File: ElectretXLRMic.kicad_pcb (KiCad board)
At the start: 2 copper layers, 37 x 52 mm, 38 parts, among them IC1 OPA1678IDR, J1 MIC, J2 XLR3

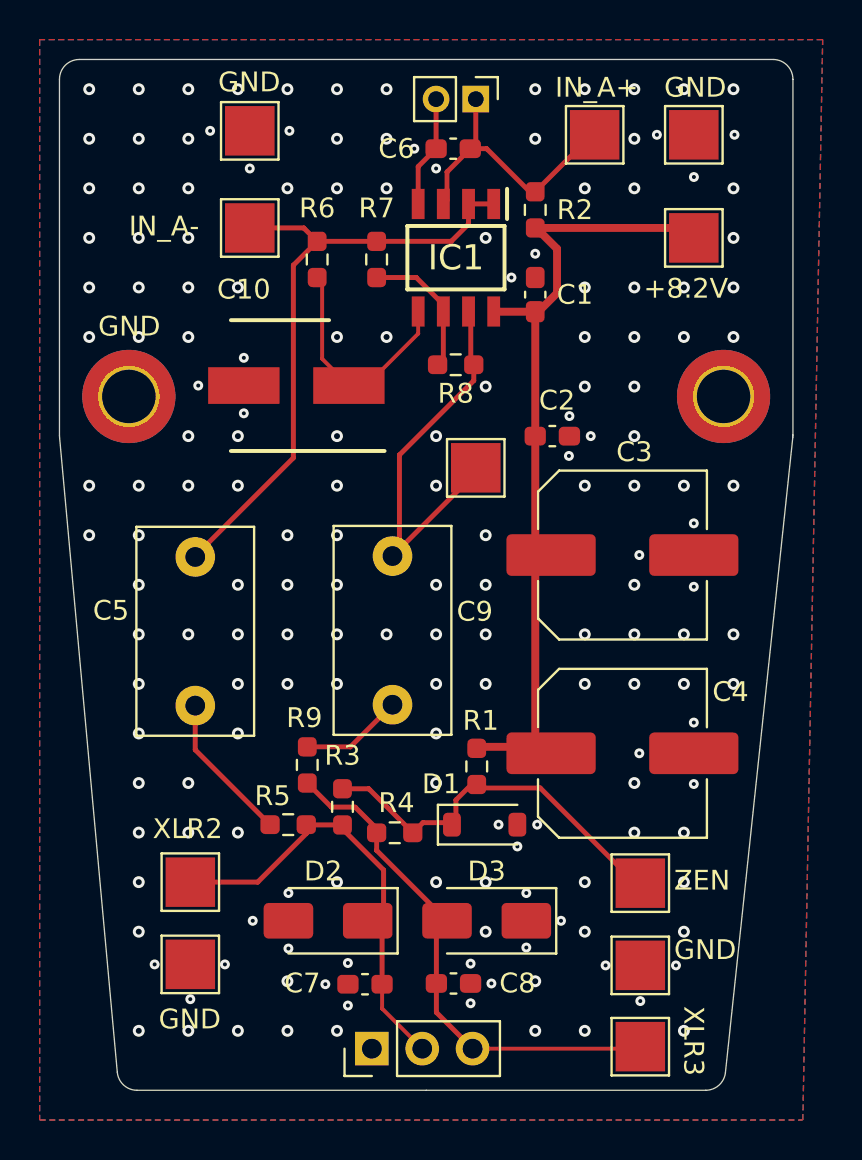
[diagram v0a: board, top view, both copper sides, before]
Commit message: Slight layout improvements
[KiCad Version: 9.0.7]
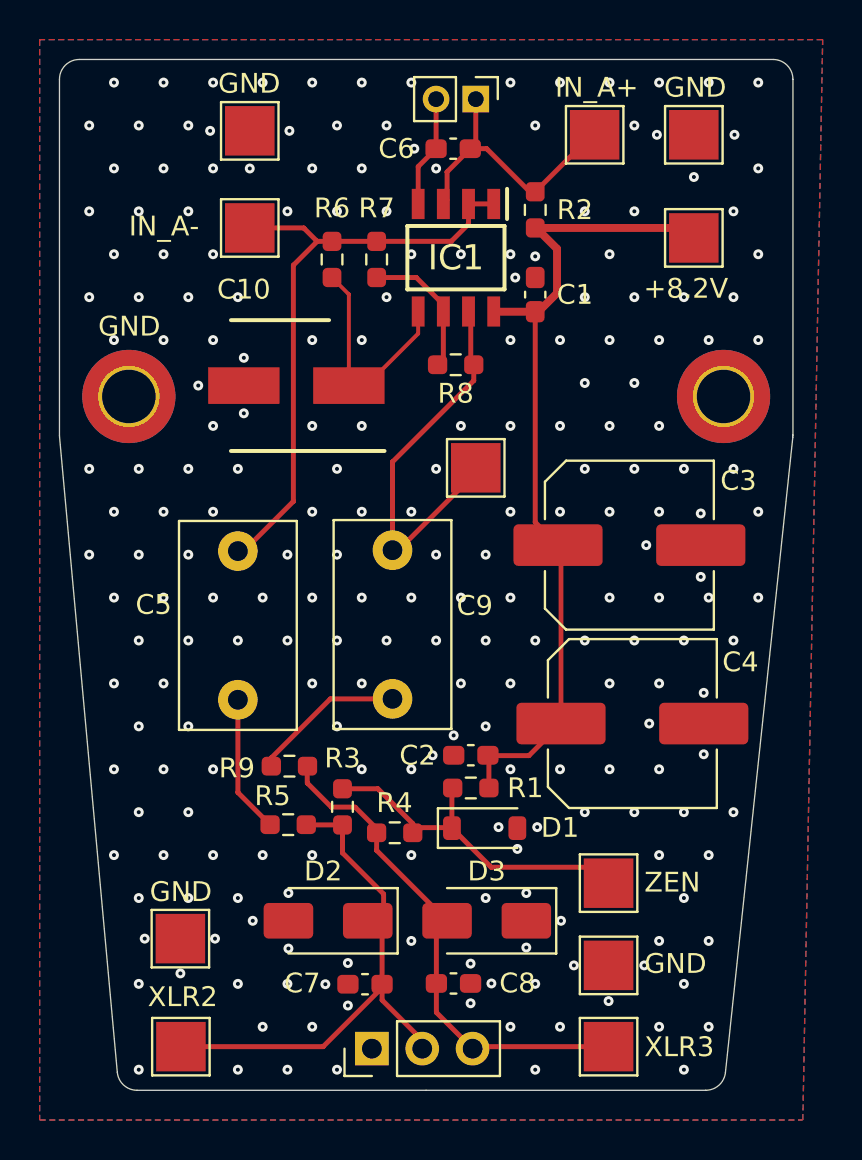
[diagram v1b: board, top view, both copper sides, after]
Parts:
- moved C2 16.6 mm to (110.8, 90.1), turned to 180 degrees
- moved TP9 8.31 mm to (96.1, 104.8)
- moved C5 2.17 mm to (99.0, 87.3)
- moved TP11 1.60 mm to (117.7, 104.8)
- moved TP2 1.60 mm to (117.7, 96.5)
- moved TP3 1.60 mm to (117.7, 100.7)
- moved C4 1.58 mm to (118.9, 88.5)
- moved TP6 1.39 mm to (96.1, 99.3)
- moved R1 1.13 mm to (110.8, 91.8), turned to 0 degrees
- moved R9 0.90 mm to (101.6, 90.7), turned to 0 degrees
- moved R6 0.75 mm to (103.8, 65.1)
- moved C3 0.61 mm to (118.8, 79.5)
- moved C9 0.30 mm to (106.8, 79.8)
- moved D1 0.18 mm to (111.5, 93.8)
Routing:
- net Net-(D2-A1): track 22.8 -> 27.0 mm
- net Net-(C9-Pad2): track 5.18 -> 8.06 mm
- net Net-(D1-K): track 19.4 -> 17.9 mm
- net Net-(C5-Pad1): track 7.61 -> 6.68 mm
- net Net-(D3-A2): track 26.5 -> 25.8 mm
- net V-: track 6.28 -> 6.13 mm, vias 177 -> 229
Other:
- board text added: "The Phantom of the Op-Amp 15.3.2026 M.H."
- board text added: "Tune OUTA to half of VCC with R2 value"
- board text removed: "The Phantom of the Op-Amp 2.3.2026 M.H."
- board text removed: "Tune OUTA to half of VCC with R2 value Match C12 and C13 closely"

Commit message: Cleaned up repo, small changes to PCB layout
[KiCad Version: 9.0.7]
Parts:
- moved TP5 28.2 mm to (94.2, 86.2)
- moved TP8 17.1 mm to (94.2, 79.8)
- moved C10 1.19 mm to (103.0, 72.0), turned to -90 degrees
- moved R9 0.97 mm to (102.5, 91.0), turned to -90 degrees
- moved C5 0.75 mm to (99.8, 87.3)
- moved C9 0.70 mm to (107.5, 79.8)
- moved TP10 0.40 mm to (111.0, 76.0)
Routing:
- net OUT_B: track 20.3 -> 13.6 mm
- net +IN_B: track 11.5 -> 9.54 mm
- net Net-(C9-Pad2): track 8.06 -> 6.17 mm
- net -IN_A: track 32.3 -> 33.6 mm
- net Net-(D3-A2): track 25.8 -> 24.7 mm
- net V-: vias 229 -> 234
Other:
- board text added: "OUTA"
- board text added: "OUTB"
- board text added: "The Phantom of the Op-Amp 17.3.2026 M.H."
- board text removed: "IN_A-"
- board text removed: "The Phantom of the Op-Amp 15.3.2026 M.H."
